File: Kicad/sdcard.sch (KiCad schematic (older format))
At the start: 0 parts

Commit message: Added SD card sheet.
Simple setup - 10k pullups, no ESD protection.
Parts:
- added C1001: 10u, symbol Device:CP
- added C1002: 100n, symbol Device:C
- added J1001: SD_Card, symbol Connector:SD_Card
- added RN1001: 8x10k, Resistor_THT:R_Array_SIP9, symbol Device:R_Network08
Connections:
- new net +3V3: C1001.1, C1002.1, J1001.4 (VDD), RN1001.1 (common)
- new net CLK: J1001.5 (CLK), RN1001.5 (R4)
- new net CMD: J1001.2 (CMD), RN1001.4 (R3)
- new net DAT0: J1001.7 (DAT0), RN1001.6 (R5)
- new net DAT1: J1001.8 (DAT1), RN1001.7 (R6)
- new net DAT2: J1001.9 (DAT2), RN1001.2 (R1)
- new net DAT3: J1001.1 (CD/DAT3), RN1001.3 (R2)
- new net GND: C1001.2, C1002.2, J1001.12 (SHELL1), J1001.13 (SHELL2), J1001.3 (VSS), J1001.6 (VSS)
- new net ~CARD_DETECT: J1001.10 (CARD_DETECT), RN1001.8 (R7)
- new net ~WRITE_PROTECT: J1001.11 (WRITE_PROTECT), RN1001.9 (R8)
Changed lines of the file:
@@
 Comment4 ""
 $EndDescr
+$Comp
+L Connector:SD_Card J1001
+U 1 1 5FE7BB6E
+P 5950 3750
+F 0 "J1001" H 5950 4415 50  0000 C CNN
+F 1 "SD_Card" H 5950 4324 50  0000 C CNN
+F 2 "" H 5950 3750 50  0001 C CNN
+F 3 "http://portal.fciconnect.com/Comergent//fci/drawing/10067847.pdf" H 5950 3750 50  0001 C CNN
+	1    5950 3750
+	1    0    0    -1
+$EndComp
+Text HLabel 3800 3350 0    50   BiDi ~ 0
+DAT2
+Text HLabel 3800 3450 0    50   BiDi ~ 0
+DAT3
+Text HLabel 3800 3550 0    50   Input ~ 0
+CMD
+Text HLabel 3800 3850 0    50   Input ~ 0
+CLK
+Text HLabel 3800 4050 0    50   BiDi ~ 0
+DAT0
+Text HLabel 3800 4150 0    50   BiDi ~ 0
+DAT1
+$Comp
+L power:+3V3 #PWR01002
+U 1 1 5FE7CAA7
+P 4800 3250
+F 0 "#PWR01002" H 4800 3100 50  0001 C CNN
+F 1 "+3V3" H 4815 3423 50  0000 C CNN
+F 2 "" H 4800 3250 50  0001 C CNN
+F 3 "" H 4800 3250 50  0001 C CNN
+	1    4800 3250
+	1    0    0    -1
+$EndComp
+Wire Wire Line
+	5050 3750 4800 3750
+Wire Wire Line
+	4800 3750 4800 3250
+$Comp
+L power:GND #PWR01005
+U 1 1 5FE7D47D
+P 4900 4250
+F 0 "#PWR01005" H 4900 4000 50  0001 C CNN
+F 1 "GND" H 4905 4077 50  0000 C CNN
+F 2 "" H 4900 4250 50  0001 C CNN
+F 3 "" H 4900 4250 50  0001 C CNN
+	1    4900 4250
+	1    0    0    -1
+$EndComp
+Wire Wire Line
+	5050 3650 4900 3650
+Wire Wire Line
+	3800 3350 3900 3350
+Wire Wire Line
+	5050 3450 4000 3450
+Wire Wire Line
+	5050 3550 4100 3550
+Wire Wire Line
+	4900 3650 4900 3950
+Wire Wire Line
+	5050 3950 4900 3950
+Connection ~ 4900 3950
+Wire Wire Line
+	4900 3950 4900 4250
+Wire Wire Line
+	3800 4050 4300 4050
+Wire Wire Line
+	5050 4150 4400 4150
+Wire Wire Line
+	3900 2700 3900 3350
+Connection ~ 3900 3350
+Wire Wire Line
+	3900 3350 5050 3350
+Wire Wire Line
+	4000 2700 4000 3450
+Connection ~ 4000 3450
+Wire Wire Line
+	4000 3450 3800 3450
+Wire Wire Line
+	4100 2700 4100 3550
+Connection ~ 4100 3550
+Wire Wire Line
+	4100 3550 3800 3550
+Wire Wire Line
+	4200 2700 4200 3850
+Connection ~ 4200 3850
+Wire Wire Line
+	4200 3850 3800 3850
+Wire Wire Line
+	4300 2700 4300 4050
+Connection ~ 4300 4050
+Wire Wire Line
+	4300 4050 5050 4050
+Wire Wire Line
+	4400 2700 4400 4150
+Connection ~ 4400 4150
+Wire Wire Line
+	4400 4150 3800 4150
+$Comp
+L power:+3V3 #PWR01001
+U 1 1 5FE8424F
+P 3900 2150
+F 0 "#PWR01001" H 3900 2000 50  0001 C CNN
+F 1 "+3V3" H 3915 2323 50  0000 C CNN
+F 2 "" H 3900 2150 50  0001 C CNN
+F 3 "" H 3900 2150 50  0001 C CNN
+	1    3900 2150
+	1    0    0    -1
+$EndComp
+Wire Wire Line
+	3900 2150 3900 2300
+$Comp
+L power:+3V3 #PWR01003
+U 1 1 5FE84AEC
+P 8250 3500
+F 0 "#PWR01003" H 8250 3350 50  0001 C CNN
+F 1 "+3V3" H 8265 3673 50  0000 C CNN
+F 2 "" H 8250 3500 50  0001 C CNN
+F 3 "" H 8250 3500 50  0001 C CNN
+	1    8250 3500
+	1    0    0    -1
+$EndComp
+$Comp
+L power:GND #PWR01004
+U 1 1 5FE84E43
+P 8250 4000
+F 0 "#PWR01004" H 8250 3750 50  0001 C CNN
+F 1 "GND" H 8255 3827 50  0000 C CNN
+F 2 "" H 8250 4000 50  0001 C CNN
+F 3 "" H 8250 4000 50  0001 C CNN
+	1    8250 4000
+	1    0    0    -1
+$EndComp
+$Comp
+L Device:CP C1001
+U 1 1 5FE85358
+P 8250 3750
+F 0 "C1001" H 8368 3796 50  0000 L CNN
+F 1 "10u" H 8368 3705 50  0000 L CNN
+F 2 "" H 8288 3600 50  0001 C CNN
+F 3 "~" H 8250 3750 50  0001 C CNN
+	1    8250 3750
+	1    0    0    -1
+$EndComp
+$Comp
+L Device:C C1002
+U 1 1 5FE86138
+P 8700 3750
+F 0 "C1002" H 8815 3796 50  0000 L CNN
+F 1 "100n" H 8815 3705 50  0000 L CNN
+F 2 "" H 8738 3600 50  0001 C CNN
+F 3 "~" H 8700 3750 50  0001 C CNN
+	1    8700 3750
+	1    0    0    -1
+$EndComp
+Wire Wire Line
+	8250 3500 8250 3550
+Wire Wire Line
+	8250 3550 8700 3550
+Wire Wire Line
+	8700 3550 8700 3600
+Connection ~ 8250 3550
+Wire Wire Line
+	8250 3550 8250 3600
+Wire Wire Line
+	8700 3900 8700 3950
+Wire Wire Line
+	8700 3950 8250 3950
+Wire Wire Line
+	8250 3950 8250 3900
+Wire Wire Line
+	8250 3950 8250 4000
+Connection ~ 8250 3950
+$Comp
+L power:GND #PWR01006
+U 1 1 5FE89E21
+P 6950 4250
+F 0 "#PWR01006" H 6950 4000 50  0001 C CNN
+F 1 "GND" H 6955 4077 50  0000 C CNN
+F 2 "" H 6950 4250 50  0001 C CNN
+F 3 "" H 6950 4250 50  0001 C CNN
+	1    6950 4250
+	1    0    0    -1
+$EndComp
+Wire Wire Line
+	6850 3950 6950 3950
+Wire Wire Line
+	6950 3950 6950 4250
+Wire Wire Line
+	6850 3850 6950 3850
+Wire Wire Line
+	6950 3850 6950 3950
+Connection ~ 6950 3950
+Wire Wire Line
+	4200 3850 5050 3850
+Text HLabel 7300 3550 2    50   Output ~ 0
+~CARD_DETECT
+Text HLabel 7300 3650 2    50   Output ~ 0
+~WRITE_PROTECT
+$Comp
+L Device:R_Network08 RN1001
+U 1 1 5FE7DE1F
+P 4300 2500
+F 0 "RN1001" H 4300 2800 50  0000 C CNN
+F 1 "8x10k" H 4300 2700 50  0000 C CNN
+F 2 "Resistor_THT:R_Array_SIP9" V 4675 2500 50  0001 C CNN
+F 3 "http://www.vishay.com/docs/31509/csc.pdf" H 4300 2500 50  0001 C CNN
+	1    4300 2500
+	1    0    0    -1
+$EndComp
+Wire Wire Line
+	6850 3550 6950 3550
+Wire Wire Line
+	6850 3650 7050 3650
+Wire Wire Line
+	4500 2700 4500 2950
+Wire Wire Line
+	4500 2950 6950 2950
+Wire Wire Line
+	6950 2950 6950 3550
+Connection ~ 6950 3550
+Wire Wire Line
+	6950 3550 7300 3550
+Wire Wire Line
+	7050 3650 7050 2850
+Wire Wire Line
+	7050 2850 4600 2850
+Wire Wire Line
+	4600 2850 4600 2700
+Connection ~ 7050 3650
+Wire Wire Line
+	7050 3650 7300 3650
 $EndSCHEMATC

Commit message: Completed PSU design.
Also changed footprint for stacked USB connector to change
shield pins from SHx to Pin 9.
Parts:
- C1001: footprint (none) -> Capacitor_THT:CP_Radial_D6.3mm_P2.50mm
- C1002: footprint (none) -> Capacitor_SMD:C_0805_2012Metric_Pad1.15x1.40mm_HandSolder
- J1001: footprint (none) -> Connector_Card:SD_Kyocera_145638109511859+
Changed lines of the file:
@@
 $Descr A4 11693 8268
 encoding utf-8
-Sheet 10 10
+Sheet 9 9
 Title "Neotron Common Hardware - SD Card Slot"
-Date "2020-12-25"
+Date "2020-12-26"
 Rev "[Uncontrolled]"
 Comp "https://neotron-compute.github.io/"
@@
 F 0 "J1001" H 5950 4415 50  0000 C CNN
 F 1 "SD_Card" H 5950 4324 50  0000 C CNN
-F 2 "" H 5950 3750 50  0001 C CNN
+F 2 "Connector_Card:SD_Kyocera_145638109511859+" H 5950 3750 50  0001 C CNN
 F 3 "http://portal.fciconnect.com/Comergent//fci/drawing/10067847.pdf" H 5950 3750 50  0001 C CNN
 	1    5950 3750
@@
 F 0 "C1001" H 8368 3796 50  0000 L CNN
 F 1 "10u" H 8368 3705 50  0000 L CNN
-F 2 "" H 8288 3600 50  0001 C CNN
+F 2 "Capacitor_THT:CP_Radial_D6.3mm_P2.50mm" H 8288 3600 50  0001 C CNN
 F 3 "~" H 8250 3750 50  0001 C CNN
 	1    8250 3750
@@
 F 0 "C1002" H 8815 3796 50  0000 L CNN
 F 1 "100n" H 8815 3705 50  0000 L CNN
-F 2 "" H 8738 3600 50  0001 C CNN
+F 2 "Capacitor_SMD:C_0805_2012Metric_Pad1.15x1.40mm_HandSolder" H 8738 3600 50  0001 C CNN
 F 3 "~" H 8700 3750 50  0001 C CNN
 	1    8700 3750

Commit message: Replaced NUC029 (TSSOP) with KE04 (SOIC).
Also updated the BOM with some part nos.
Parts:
- C1001: DNP (none) -> 0; Digikey (none) -> 493-10359-1-ND; MPN (none) -> UMW1E100MDD1TP; Manufacturer (none) -> Nichicon
- C1002: DNP (none) -> 0; Digikey (none) -> BC1150CT-ND; MPN (none) -> K104K15X7RF5TL2; Manufacturer (none) -> Vishay
- J1001, RN1001: DNP (none) -> 0
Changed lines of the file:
@@
 F 2 "Connector_Card:SD_Kyocera_145638109511859+" H 5950 3750 50  0001 C CNN
 F 3 "http://portal.fciconnect.com/Comergent//fci/drawing/10067847.pdf" H 5950 3750 50  0001 C CNN
+F 4 "0" H 5950 3750 50  0001 C CNN "DNP"
 	1    5950 3750
 	1    0    0    -1
@@
 F 2 "Capacitor_THT:CP_Radial_D6.3mm_P2.50mm" H 8288 3600 50  0001 C CNN
 F 3 "~" H 8250 3750 50  0001 C CNN
+F 4 "0" H 8250 3750 50  0001 C CNN "DNP"
+F 5 "493-10359-1-ND" H 8250 3750 50  0001 C CNN "Digikey"
+F 6 "UMW1E100MDD1TP" H 8250 3750 50  0001 C CNN "MPN"
+F 7 "Nichicon" H 8250 3750 50  0001 C CNN "Manufacturer"
 	1    8250 3750
 	1    0    0    -1
@@
 F 2 "Capacitor_SMD:C_0805_2012Metric_Pad1.15x1.40mm_HandSolder" H 8738 3600 50  0001 C CNN
 F 3 "~" H 8700 3750 50  0001 C CNN
+F 4 "0" H 8700 3750 50  0001 C CNN "DNP"
+F 5 "BC1150CT-ND" H 8700 3750 50  0001 C CNN "Digikey"
+F 6 "K104K15X7RF5TL2" H 8700 3750 50  0001 C CNN "MPN"
+F 7 "Vishay" H 8700 3750 50  0001 C CNN "Manufacturer"
 	1    8700 3750
 	1    0    0    -1
@@
 F 2 "Resistor_THT:R_Array_SIP9" V 4675 2500 50  0001 C CNN
 F 3 "http://www.vishay.com/docs/31509/csc.pdf" H 4300 2500 50  0001 C CNN
+F 4 "0" H 4300 2500 50  0001 C CNN "DNP"
 	1    4300 2500
 	1    0    0    -1

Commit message: Changed CPU socket to be 2x20 x2. Added expansion slots.
Also added 3D model for the SD card.
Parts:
- J1001: footprint Connector_Card:SD_Kyocera_145638109511859+ -> Connector_Card:SD_Kyocera_145638009211859+
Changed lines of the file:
@@
 F 0 "J1001" H 5950 4415 50  0000 C CNN
 F 1 "SD_Card" H 5950 4324 50  0000 C CNN
-F 2 "Connector_Card:SD_Kyocera_145638109511859+" H 5950 3750 50  0001 C CNN
+F 2 "Connector_Card:SD_Kyocera_145638009211859+" H 5950 3750 50  0001 C CNN
 F 3 "http://portal.fciconnect.com/Comergent//fci/drawing/10067847.pdf" H 5950 3750 50  0001 C CNN
 F 4 "0" H 5950 3750 50  0001 C CNN "DNP"

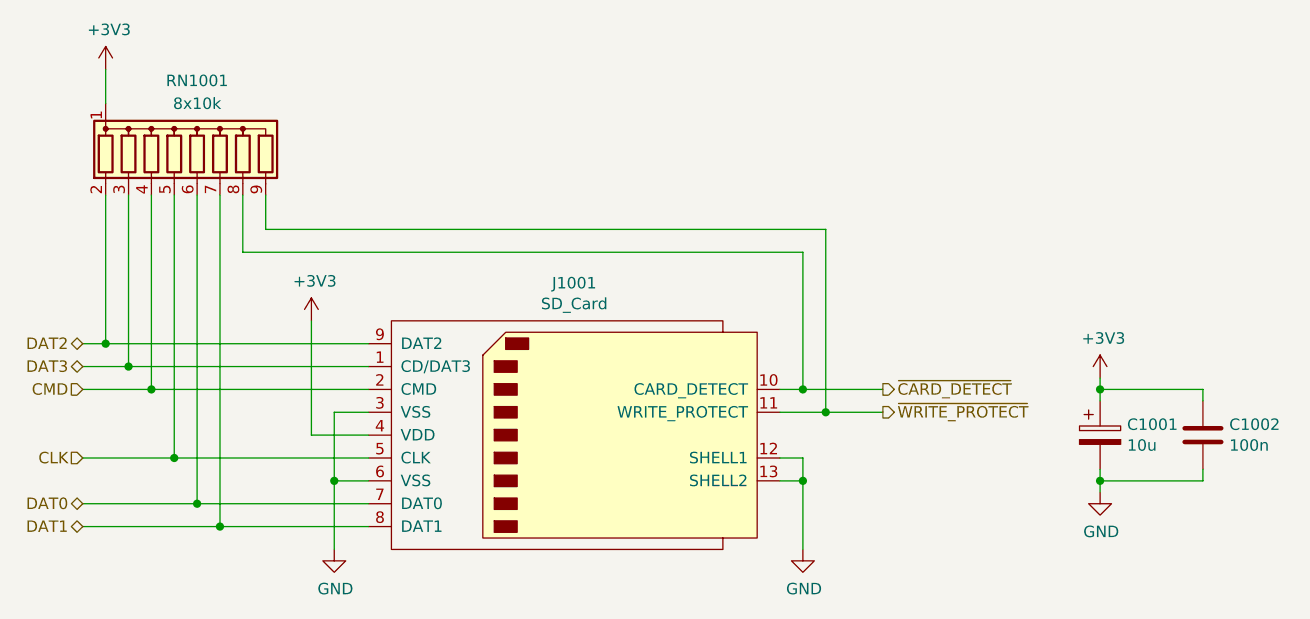
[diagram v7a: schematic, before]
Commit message: Bring in R2R DAC from Neotron-9X schematic.
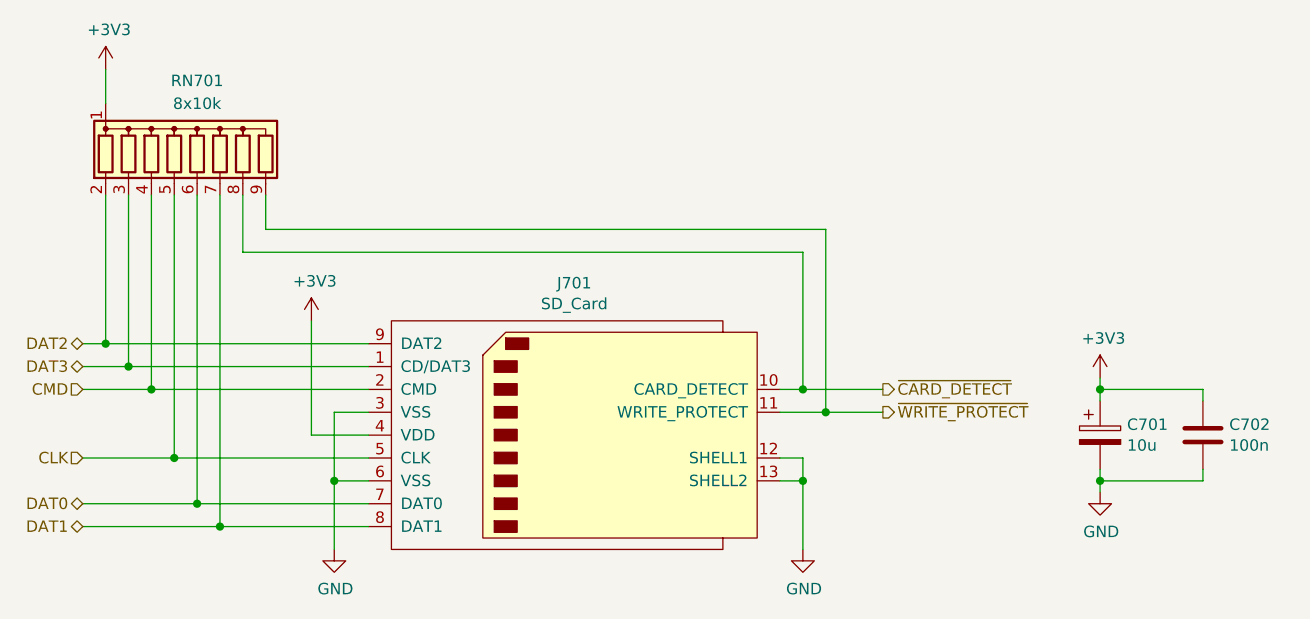
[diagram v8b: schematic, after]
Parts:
- renumbered C1001 to C701, C1002 to C702, J1001 to J701, RN1001 to RN701
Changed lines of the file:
@@
 $Descr A4 11693 8268
 encoding utf-8
-Sheet 4 9
+Sheet 4 12
 Title "Neotron Common Hardware - SD Card Slot"
 Date "2021-01-01"
@@
 $EndDescr
 $Comp
-L Connector:SD_Card J1001
+L Connector:SD_Card J701
 U 1 1 5FE7BB6E
 P 5950 3750
-F 0 "J1001" H 5950 4415 50  0000 C CNN
+F 0 "J701" H 5950 4415 50  0000 C CNN
 F 1 "SD_Card" H 5950 4324 50  0000 C CNN
 F 2 "Connector_Card:SD_Kyocera_145638009211859+" H 5950 3750 50  0001 C CNN
@@
 DAT1
 $Comp
-L power:+3V3 #PWR01002
+L power:+3V3 #PWR0702
 U 1 1 5FE7CAA7
 P 4800 3250
-F 0 "#PWR01002" H 4800 3100 50  0001 C CNN
+F 0 "#PWR0702" H 4800 3100 50  0001 C CNN
 F 1 "+3V3" H 4815 3423 50  0000 C CNN
 F 2 "" H 4800 3250 50  0001 C CNN
@@
 	4800 3750 4800 3250
 $Comp
-L power:GND #PWR01005
+L power:GND #PWR0705
 U 1 1 5FE7D47D
 P 4900 4250
-F 0 "#PWR01005" H 4900 4000 50  0001 C CNN
+F 0 "#PWR0705" H 4900 4000 50  0001 C CNN
 F 1 "GND" H 4905 4077 50  0000 C CNN
 F 2 "" H 4900 4250 50  0001 C CNN
@@
 	4400 4150 3800 4150
 $Comp
-L power:+3V3 #PWR01001
+L power:+3V3 #PWR0701
 U 1 1 5FE8424F
 P 3900 2150
-F 0 "#PWR01001" H 3900 2000 50  0001 C CNN
+F 0 "#PWR0701" H 3900 2000 50  0001 C CNN
 F 1 "+3V3" H 3915 2323 50  0000 C CNN
 F 2 "" H 3900 2150 50  0001 C CNN
@@
 	3900 2150 3900 2300
 $Comp
-L power:+3V3 #PWR01003
+L power:+3V3 #PWR0703
 U 1 1 5FE84AEC
 P 8250 3500
-F 0 "#PWR01003" H 8250 3350 50  0001 C CNN
+F 0 "#PWR0703" H 8250 3350 50  0001 C CNN
 F 1 "+3V3" H 8265 3673 50  0000 C CNN
 F 2 "" H 8250 3500 50  0001 C CNN
@@
 $EndComp
 $Comp
-L power:GND #PWR01004
+L power:GND #PWR0704
 U 1 1 5FE84E43
 P 8250 4000
-F 0 "#PWR01004" H 8250 3750 50  0001 C CNN
+F 0 "#PWR0704" H 8250 3750 50  0001 C CNN
 F 1 "GND" H 8255 3827 50  0000 C CNN
 F 2 "" H 8250 4000 50  0001 C CNN
@@
 $EndComp
 $Comp
-L Device:CP C1001
+L Device:CP C701
 U 1 1 5FE85358
 P 8250 3750
-F 0 "C1001" H 8368 3796 50  0000 L CNN
+F 0 "C701" H 8368 3796 50  0000 L CNN
 F 1 "10u" H 8368 3705 50  0000 L CNN
 F 2 "Capacitor_THT:CP_Radial_D6.3mm_P2.50mm" H 8288 3600 50  0001 C CNN
@@
 $EndComp
 $Comp
-L Device:C C1002
+L Device:C C702
 U 1 1 5FE86138
 P 8700 3750
-F 0 "C1002" H 8815 3796 50  0000 L CNN
+F 0 "C702" H 8815 3796 50  0000 L CNN
 F 1 "100n" H 8815 3705 50  0000 L CNN
 F 2 "Capacitor_SMD:C_0805_2012Metric_Pad1.15x1.40mm_HandSolder" H 8738 3600 50  0001 C CNN
@@
 Connection ~ 8250 3950
 $Comp
-L power:GND #PWR01006
+L power:GND #PWR0706
 U 1 1 5FE89E21
 P 6950 4250
-F 0 "#PWR01006" H 6950 4000 50  0001 C CNN
+F 0 "#PWR0706" H 6950 4000 50  0001 C CNN
 F 1 "GND" H 6955 4077 50  0000 C CNN
 F 2 "" H 6950 4250 50  0001 C CNN
@@
 ~WRITE_PROTECT
 $Comp
-L Device:R_Network08 RN1001
+L Device:R_Network08 RN701
 U 1 1 5FE7DE1F
 P 4300 2500
-F 0 "RN1001" H 4300 2800 50  0000 C CNN
+F 0 "RN701" H 4300 2800 50  0000 C CNN
 F 1 "8x10k" H 4300 2700 50  0000 C CNN
 F 2 "Resistor_THT:R_Array_SIP9" V 4675 2500 50  0001 C CNN
